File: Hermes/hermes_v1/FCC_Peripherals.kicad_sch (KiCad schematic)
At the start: 26 parts, among them J2 Connector_USB_B_Micro, J3 Conn_01x07, J4 Conn_02x07_Odd_Even, J5 Additional IO, J6 Micro_SD_Card, J7 IO Power, U5 MPU-6050, U6 MPL3115A2, U7 USBLC6-2P6

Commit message: Hermes v2
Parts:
- removed C21, C24: 0.1uF, Capacitor_SMD:C_0402_1005Metric_Pad0.74x0.62mm_HandSolder, symbol Device:C_Small
- removed C23: 10uF, Capacitor_SMD:C_0402_1005Metric_Pad0.74x0.62mm_HandSolder, symbol Device:C_Small
- removed J3: Conn_01x07, Connector_PinHeader_2.54mm:PinHeader_1x07_P2.54mm_Vertical, symbol Connector_Generic:Conn_01x07
- removed J4: Conn_02x07_Odd_Even, Connector_PinHeader_2.54mm:PinHeader_2x07_P2.54mm_Vertical, symbol Connector_Generic:Conn_02x07_Odd_Even
- removed J5: Additional IO, Connector_PinHeader_2.54mm:PinHeader_2x03_P2.54mm_Vertical, symbol Connector_Generic:Conn_02x03_Odd_Even
- removed J7: IO Power, Connector_PinHeader_2.54mm:PinHeader_2x03_P2.54mm_Vertical, symbol Connector_Generic:Conn_02x03_Odd_Even
- removed U6: MPL3115A2, Package_LGA:NXP_LGA-8_3x5mm_P1.25mm_H1.1mm, symbol Sensor_Pressure:MPL3115A2
- added J1: Conn_02x20_Odd_Even, Connector_PinSocket_2.54mm:PinSocket_2x20_P2.54mm_Vertical, symbol Connector_Generic:Conn_02x20_Odd_Even
- added J3: Conn_02x04_Odd_Even, Connector_PinHeader_2.54mm:PinHeader_2x04_P2.54mm_Vertical, symbol Connector_Generic:Conn_02x04_Odd_Even
- added J8: Conn_01x08, Connector_PinHeader_2.54mm:PinHeader_1x08_P2.54mm_Vertical, symbol Connector_Generic:Conn_01x08
- added J9: Conn_02x08_Odd_Even, Connector_PinHeader_2.54mm:PinHeader_2x08_P2.54mm_Vertical, symbol Connector_Generic:Conn_02x08_Odd_Even
- J2: footprint Connector_USB:USB_Micro-B_Wuerth_614105150721_Vertical -> Connector_USB:USB_Micro-B_Amphenol_10118194_Horizontal
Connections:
- net +5V: now also J3.7 (Pin_7), J9.10 (Pin_10), J9.12 (Pin_12), J9.14 (Pin_14), J9.16 (Pin_16), J9.2 (Pin_2), J9.4 (Pin_4), J9.6 (Pin_6), J9.8 (Pin_8)
- net 3V3_IO: now also J3.8 (Pin_8)
- net FC_RADIO_PPM: now also J8.8 (Pin_8)
- net FC_SERVO_1: now also J8.1 (Pin_1)
- net FC_SERVO_2: now also J8.2 (Pin_2)
- net FC_SERVO_3: now also J8.3 (Pin_3)
- net FC_SERVO_4: now also J8.4 (Pin_4)
- net FC_SERVO_5: now also J8.5 (Pin_5)
- net FC_SERVO_6: now also J8.6 (Pin_6)
- net FC_UART0_RX: now also J3.3 (Pin_3)
- net FC_UART0_TX: now also J3.5 (Pin_5)
- net FC_UART1_RX: now also J3.4 (Pin_4)
- net FC_UART1_TX: now also J3.6 (Pin_6)
- net GND: now also J3.1 (Pin_1), J3.2 (Pin_2), J9.1 (Pin_1), J9.11 (Pin_11), J9.13 (Pin_13), J9.15 (Pin_15), J9.3 (Pin_3), J9.5 (Pin_5), J9.7 (Pin_7), J9.9 (Pin_9)
- new net FC_SERVO_7: J8.7 (Pin_7)
- no-connect marks 9 -> 7
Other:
- note removed: "Barometric Pressure Sensor"

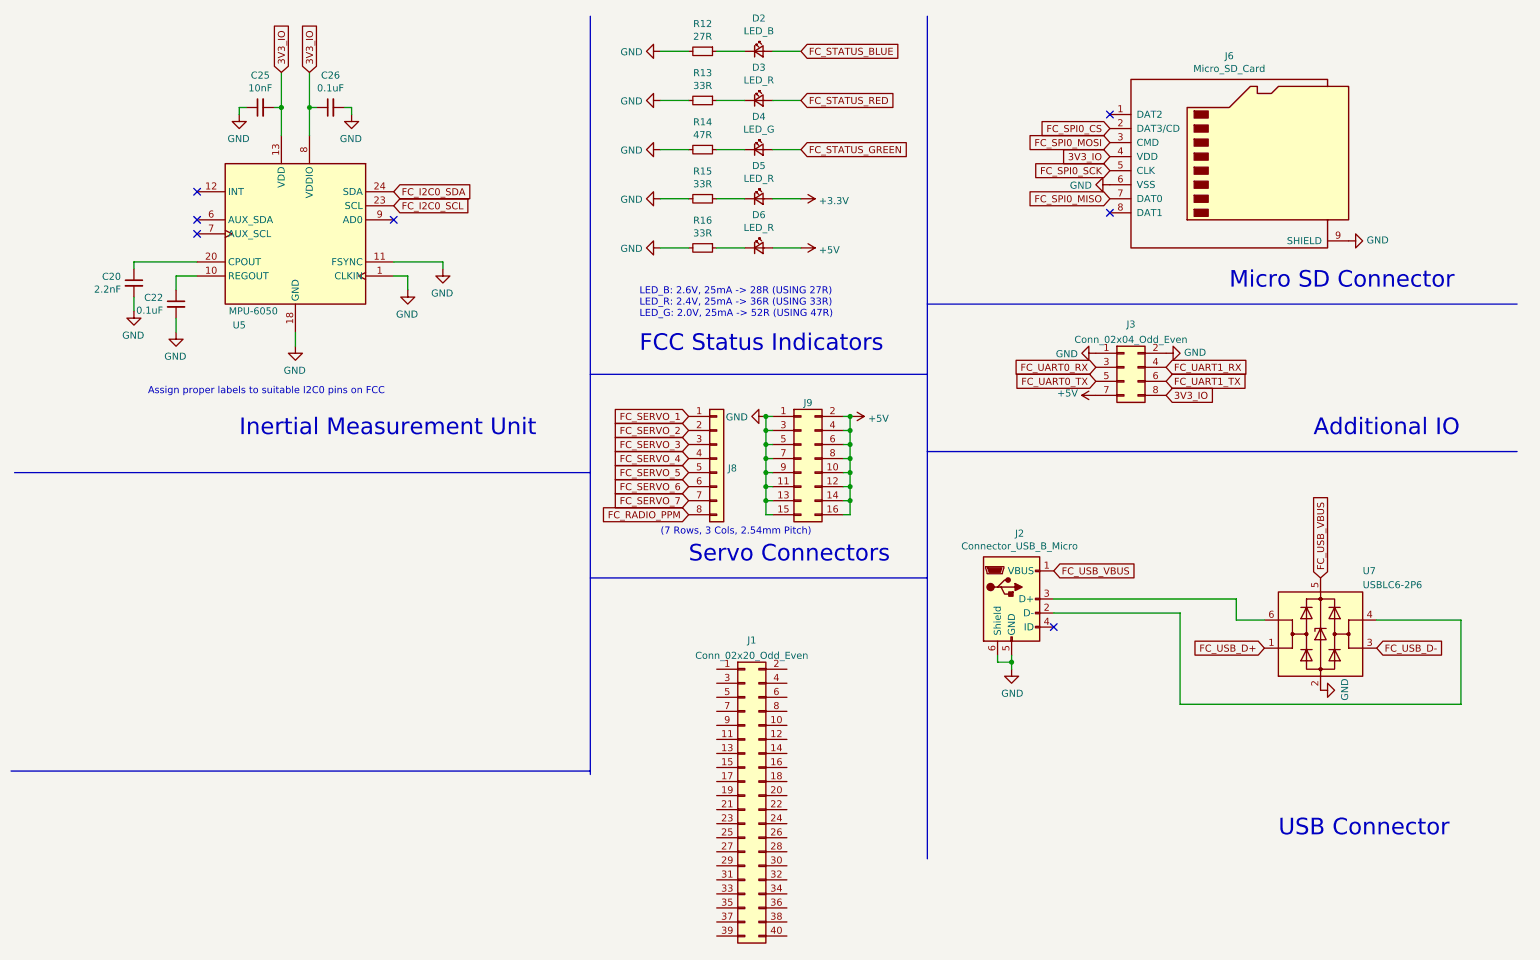
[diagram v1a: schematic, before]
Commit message: Added VoltPak 1000
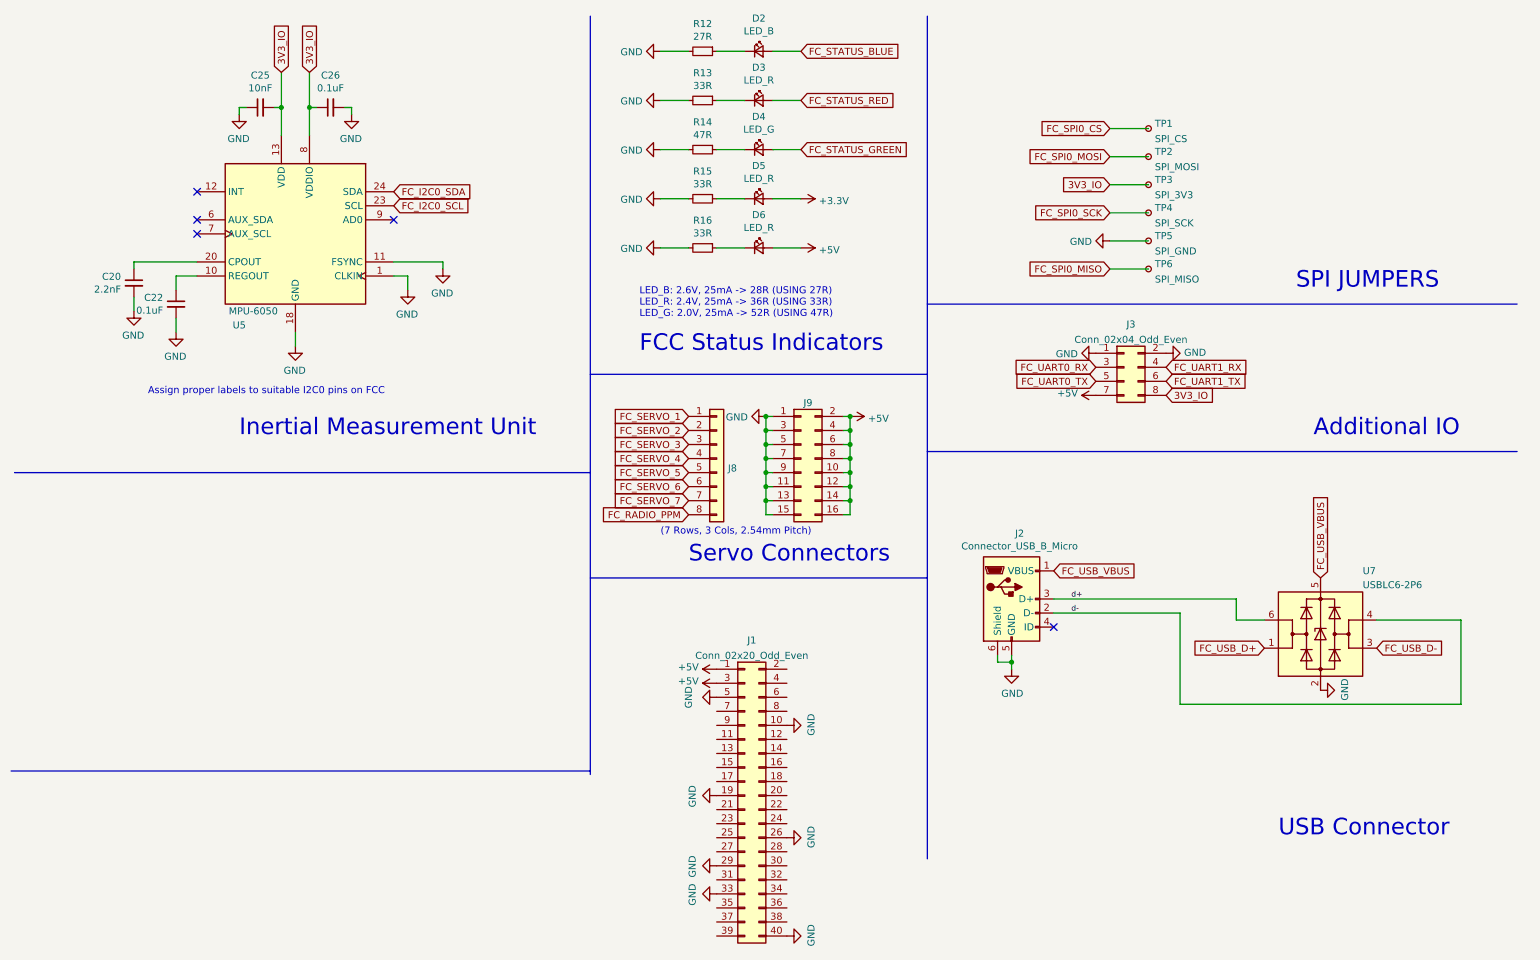
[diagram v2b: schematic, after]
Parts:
- removed J6: Micro_SD_Card, Connector_Card:microSD_HC_Wuerth_693072010801, symbol Connector:Micro_SD_Card
- added TP1: SPI_CS, TestPoint:TestPoint_Pad_D1.0mm, symbol Connector:TestPoint_Small
- added TP2: SPI_MOSI, TestPoint:TestPoint_Pad_D1.0mm, symbol Connector:TestPoint_Small
- added TP3: SPI_3V3, TestPoint:TestPoint_Pad_D1.0mm, symbol Connector:TestPoint_Small
- added TP4: SPI_SCK, TestPoint:TestPoint_Pad_D1.0mm, symbol Connector:TestPoint_Small
- added TP5: SPI_GND, TestPoint:TestPoint_Pad_D1.0mm, symbol Connector:TestPoint_Small
- added TP6: SPI_MISO, TestPoint:TestPoint_Pad_D1.0mm, symbol Connector:TestPoint_Small
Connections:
- net +5V: now also J1.1 (Pin_1), J1.3 (Pin_3)
- net 3V3_IO: now also TP3.1
- net FC_SPI0_CS: now also TP1.1
- net FC_SPI0_MISO: now also TP6.1
- net FC_SPI0_MOSI: now also TP2.1
- net FC_SPI0_SCK: now also TP4.1
- net GND: now also J1.10 (Pin_10), J1.19 (Pin_19), J1.26 (Pin_26), J1.29 (Pin_29), J1.33 (Pin_33), J1.40 (Pin_40), J1.5 (Pin_5), TP5.1
- net d-: now reaches J2.2 (D-), U7.4 (I/O2)
- net d+: now reaches J2.3 (D+), U7.6 (I/O1)
- no-connect marks 7 -> 5
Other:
- note added: "SPI JUMPERS"
- note removed: "Micro SD Connector"
